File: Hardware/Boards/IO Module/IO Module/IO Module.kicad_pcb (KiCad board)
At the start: 8 copper layers, 50 x 50 mm, 301 parts, among them J1 USB_C_Receptacle, J2 LSHM-130-XX.X-XXX-DV-A-S-K-XX, J3 LSHM-130-XX.X-XXX-DV-A-S-K-XX, J4 HDMI_A, J5 Cam FPC, Q1 IRLML6244, Q2 IRLML6244, SW1 RST, U1 TPS25730D, U10 74LVC1G97, U11 93LCxxBxxOT, U12 74AVC2T245GU, U13 FT600Q, U14 W25Q16JVUXIQ TR, U15 RP2040, U16 TPS74801AWDRC, U17 TUSB542, U18 TUSB8041, U19 TPS74801AWDRC, U2 INA700AYWFR, U20 SN75DP159RGZ, U21 TXB0108DQSR, U22 TXB0101DCK, U23 SN65DPHY440SS, U3 TPSM33625RDNR, U4 TPD2EUSB30A, U5 TPD4EUSB30, U6 TPSM33625RDNR, U7 TPD4EUSB30, U8 74AVC4T774BQX, U9 FT2232HQ, Y1 12Mhz, Y2 30Mhz, Y3 12Mhz, Y4 24Mhz

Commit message: PCB Layout Started
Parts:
- added R103: 1.6K, Resistor_SMD:R_0402_1005Metric, F.Cu at (36.5, 160.0)
- J1: footprint Connector_USB:USB_C_Receptacle_Amphenol_12401548E4-2A -> Connector_USB:USB_C_Receptacle_Amphenol_12401610E4-2A
- J2, J3: moved to B.Cu
- moved U17 130.3 mm to (152.0, 105.0), turned to 90 degrees
- moved U18 125.8 mm to (163.4, 106.4)
- moved J3 123.1 mm to (173.0, 96.0), turned to 90 degrees
- moved J1 119.8 mm to (152.0, 116.0)
- moved U7 109.2 mm to (154.7, 108.2), turned to -90 degrees
- moved U4 108.9 mm to (152.0, 108.3), turned to 180 degrees
- moved U5 106.8 mm to (149.3, 108.3), turned to -90 degrees
- moved U1 97.4 mm to (141.6, 113.1)
- moved J2 84.2 mm to (131.0, 96.0), turned to -90 degrees
- moved TP4 74.9 mm to (174.8, 118.8)
- moved U23 71.3 mm to (163.6, 81.4), turned to 90 degrees
- moved J5 69.7 mm to (162.0, 74.7), turned to 180 degrees
- moved J4 68.4 mm to (142.0, 77.7), turned to 90 degrees
- moved U20 67.2 mm to (140.1, 88.6), turned to 90 degrees
- moved TP2 64.9 mm to (174.8, 73.2)
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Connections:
- U13 pad 21: (no net) -> Net-(U13-RREF)

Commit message: Updated SCH with notes & annotations
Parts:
- removed Q2: IRLML6244, Package_TO_SOT_SMD:SOT-23
- removed U17: TUSB542, IO_Module:TUSB542
- added C149: 100nF, Capacitor_SMD:C_0402_1005Metric, F.Cu at (193.3, 121.5)
- added C150: 100nF, Capacitor_SMD:C_0402_1005Metric, F.Cu at (193.3, 123.5)
- added C151: 100nF, Capacitor_SMD:C_0402_1005Metric, F.Cu at (193.3, 125.4)
- added C152: 100nF, Capacitor_SMD:C_0402_1005Metric, F.Cu at (193.3, 127.4)
- added R104: 1K, Resistor_SMD:R_0402_1005Metric, F.Cu at (184.6, 121.5)
- added R105: 1K, Resistor_SMD:R_0402_1005Metric, F.Cu at (184.6, 123.5)
- added R106: 1K, Resistor_SMD:R_0402_1005Metric, F.Cu at (184.6, 125.5)
- added R107: 1K, Resistor_SMD:R_0402_1005Metric, F.Cu at (184.6, 127.5)
- added R108: 1K, Resistor_SMD:R_0402_1005Metric, F.Cu at (184.6, 129.5)
- added R109: 1K, Resistor_SMD:R_0402_1005Metric, F.Cu at (187.5, 121.5)
- added R110: 1K, Resistor_SMD:R_0402_1005Metric, F.Cu at (187.5, 123.5)
- added R111: 1K, Resistor_SMD:R_0402_1005Metric, F.Cu at (187.5, 125.5)
- added R112: 1K, Resistor_SMD:R_0402_1005Metric, F.Cu at (187.5, 127.5)
- added R113: 1K, Resistor_SMD:R_0402_1005Metric, F.Cu at (187.5, 129.5)
- added R114: 1K, Resistor_SMD:R_0402_1005Metric, F.Cu at (190.4, 121.5)
- added R115: 1K, Resistor_SMD:R_0402_1005Metric, F.Cu at (190.4, 123.5)
- added R116: 1K, Resistor_SMD:R_0402_1005Metric, F.Cu at (190.4, 125.5)
- added R117: 1K, Resistor_SMD:R_0402_1005Metric, F.Cu at (190.4, 127.5)
- added U24: TUSB1142, IO_Module:WQFN_142RNQT_TEX, F.Cu at (155.7, 103.6)
- C101, C102, C103, C105, C106, C107, C108, C94: value 100nF -> 220nF
- C109: value 1uF -> 10uF; footprint Capacitor_SMD:C_0402_1005Metric -> Capacitor_SMD:C_0603_1608Metric
- J1: footprint Connector_USB:USB_C_Receptacle_Amphenol_12401610E4-2A -> IO_Module:GCT_USB4056-03-A_REVA2
- R64, R65, R66, R69: value 10K -> 1K
- moved U3 151.8 mm to (184.2, 115.6)
- moved U6 151.8 mm to (190.1, 115.6)
- moved U10 134.5 mm to (195.8, 101.0), turned to 90 degrees
- moved C108 131.6 mm to (164.1, 108.1), turned to 90 degrees
- moved C102 130.9 mm to (160.3, 108.0), turned to 90 degrees
- moved C107 130.8 mm to (163.4, 108.1), turned to 90 degrees
- moved C105 130.7 mm to (159.7, 108.0), turned to 90 degrees
- moved U12 129.5 mm to (190.4, 95.0), turned to 180 degrees
- moved U2 128.1 mm to (170.7, 110.5), turned to 180 degrees
- moved U8 126.7 mm to (196.7, 105.2), turned to -90 degrees
- moved C106 123.3 mm to (151.8, 107.8), turned to -90 degrees
- moved C94 123.1 mm to (149.7, 107.8), turned to -90 degrees
- moved C103 121.9 mm to (151.2, 107.8), turned to -90 degrees
- moved C101 120.8 mm to (150.3, 107.8), turned to -90 degrees
- moved Y2 120.4 mm to (142.0, 116.5), turned to 90 degrees
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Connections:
- C109 pad 1: +1V8 -> +3V3
- J2 pad 34: /Top/B2B/FIFO_BE0 -> GND
- J2 pad 36: /Top/B2B/FIFO_BE1 -> GND
- J3 pad 01: /Top/B2B/FIFO_CLK -> /Top/B2B/FIFO_BE0
- J3 pad 03: /Top/B2B/FIFO_D0 -> /Top/B2B/FIFO_BE1
- J3 pad 05: /Top/B2B/FIFO_D1 -> /Top/B2B/FIFO_CLK
- J3 pad 07: /Top/B2B/FIFO_D2 -> /Top/B2B/FIFO_D0
- J3 pad 09: /Top/B2B/FIFO_D3 -> /Top/B2B/FIFO_D1
- J3 pad 11: /Top/B2B/FIFO_D4 -> /Top/B2B/FIFO_D2
- J3 pad 13: /Top/B2B/FIFO_D5 -> /Top/B2B/FIFO_D3
- J3 pad 15: /Top/B2B/FIFO_D6 -> /Top/B2B/FIFO_D4
- J3 pad 17: /Top/B2B/FIFO_D7 -> /Top/B2B/FIFO_D5
- J3 pad 19: GND -> /Top/B2B/FIFO_D6
- J3 pad 21: /Top/B2B/MBUS_D0 -> /Top/B2B/FIFO_D7
- J3 pad 23: /Top/B2B/MBUS_D1 -> GND
- J3 pad 25: /Top/B2B/MBUS_D2 -> /Top/B2B/MBUS_D0
- J3 pad 27: /Top/B2B/MBUS_D3 -> /Top/B2B/MBUS_D1
- J3 pad 29: /Top/B2B/MBUS_D4 -> /Top/B2B/MBUS_D2
- J3 pad 31: /Top/B2B/MBUS_D5 -> /Top/B2B/MBUS_D3
- J3 pad 33: /Top/B2B/MBUS_D6 -> /Top/B2B/MBUS_D4
- J3 pad 35: /Top/B2B/MBUS_D7 -> /Top/B2B/MBUS_D5
- J3 pad 37: GND -> /Top/B2B/MBUS_D6
- J3 pad 39: /Top/B2B/MIPI_D0_P -> /Top/B2B/MBUS_D7
- J3 pad 41: /Top/B2B/MIPI_D0_N -> GND
- J3 pad 43: GND -> /Top/B2B/MIPI_D0_P
- J3 pad 45: /Top/B2B/MIPI_D1_P -> /Top/B2B/MIPI_D0_N
- J3 pad 47: /Top/B2B/MIPI_D1_N -> GND
- J3 pad 49: GND -> /Top/B2B/MIPI_D1_P
- J3 pad 51: /Top/B2B/MIPI_CLK_P -> /Top/B2B/MIPI_D1_N
- J3 pad 53: /Top/B2B/MIPI_CLK_N -> GND
- J3 pad 55: GND -> /Top/B2B/MIPI_CLK_P
- J3 pad 57: GND -> /Top/B2B/MIPI_CLK_N
- J4 pad 1: /Top/HDMI/HDMI_C_D2_P -> /Top/HDMI/HDMI_CON_D2_P
- J4 pad 10: /Top/HDMI/HDMI_C_CLK_P -> /Top/HDMI/HDMI_CON_CLK_P
- J4 pad 12: /Top/HDMI/HDMI_C_CLK_N -> /Top/HDMI/HDMI_CON_CLK_N
- J4 pad 3: /Top/HDMI/HDMI_C_D2_N -> /Top/HDMI/HDMI_CON_D2_N
- J4 pad 4: /Top/HDMI/HDMI_C_D1_P -> /Top/HDMI/HDMI_CON_D1_P
- J4 pad 6: /Top/HDMI/HDMI_C_D1_N -> /Top/HDMI/HDMI_CON_D1_N
- J4 pad 7: /Top/HDMI/HDMI_C_D0_P -> /Top/HDMI/HDMI_CON_D0_P
- J4 pad 9: /Top/HDMI/HDMI_C_D0_N -> /Top/HDMI/HDMI_CON_D0_N
- R64 pad 1: Net-(U17-CFG_B2) -> GND
- R64 pad 2: +1V8 -> /Top/USB Hub/USSEQ1
- R65 pad 1: Net-(Q2-D) -> /Top/USB Hub/USSEQ1
- R65 pad 2: +1V8 -> +3V3
- R66 pad 1: GND -> /Top/USB Hub/USSEQ0
- R66 pad 2: Net-(U17-CFG_B2) -> +3V3
- R69 pad 2: /Top/MCU/USBPD_PLG_FLIP -> /Top/USB Hub/USSEQ0
- U20 pad 25: /Top/HDMI/HDMI_C_CLK_N -> /Top/HDMI/HDMI_CON_CLK_N
- U20 pad 26: /Top/HDMI/HDMI_C_CLK_P -> /Top/HDMI/HDMI_CON_CLK_P
- U20 pad 28: /Top/HDMI/HDMI_C_D0_N -> /Top/HDMI/HDMI_CON_D0_N
- U20 pad 29: /Top/HDMI/HDMI_C_D0_P -> /Top/HDMI/HDMI_CON_D0_P
- U20 pad 31: /Top/HDMI/HDMI_C_D1_N -> /Top/HDMI/HDMI_CON_D1_N
- U20 pad 32: /Top/HDMI/HDMI_C_D1_P -> /Top/HDMI/HDMI_CON_D1_P
- U20 pad 34: /Top/HDMI/HDMI_C_D2_N -> /Top/HDMI/HDMI_CON_D2_N
- U20 pad 35: /Top/HDMI/HDMI_C_D2_P -> /Top/HDMI/HDMI_CON_D2_P
- U5 pad 1: /Top/Power/USB3_RX1_P -> /Top/Power/USB3_TX1_N
- U5 pad 10: /Top/Power/USB3_RX1_P -> /Top/Power/USB3_TX1_N
- U5 pad 2: /Top/Power/USB3_RX1_N -> /Top/Power/USB3_TX1_P
- U5 pad 4: /Top/Power/USB3_TX1_P -> /Top/Power/USB3_RX1_N
- U5 pad 5: /Top/Power/USB3_TX1_N -> /Top/Power/USB3_RX1_P
- U5 pad 6: /Top/Power/USB3_TX1_N -> /Top/Power/USB3_RX1_P
- U5 pad 7: /Top/Power/USB3_TX1_P -> /Top/Power/USB3_RX1_N
- U5 pad 9: /Top/Power/USB3_RX1_N -> /Top/Power/USB3_TX1_P
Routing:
- net GND: track 0.00 -> 0.39 mm, vias 0 -> 1
- added copper zone on In1.Cu, net (none)
- added copper zone on In3.Cu, net (none)
- added copper zone on In4.Cu, net (none)
- added copper zone on In6.Cu, net (none)

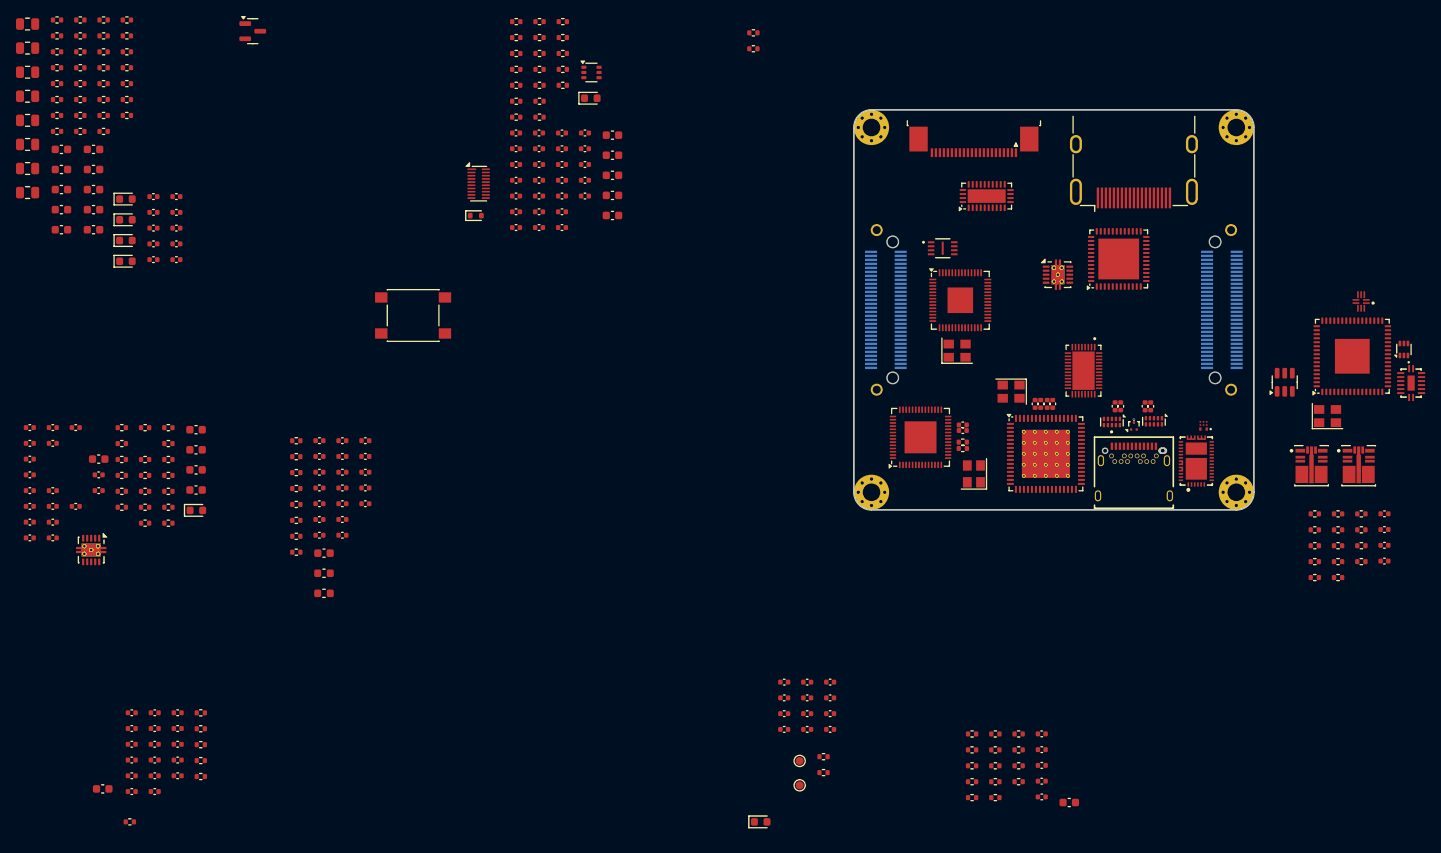
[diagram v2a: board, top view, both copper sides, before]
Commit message: Updated PCB routing for IO Module
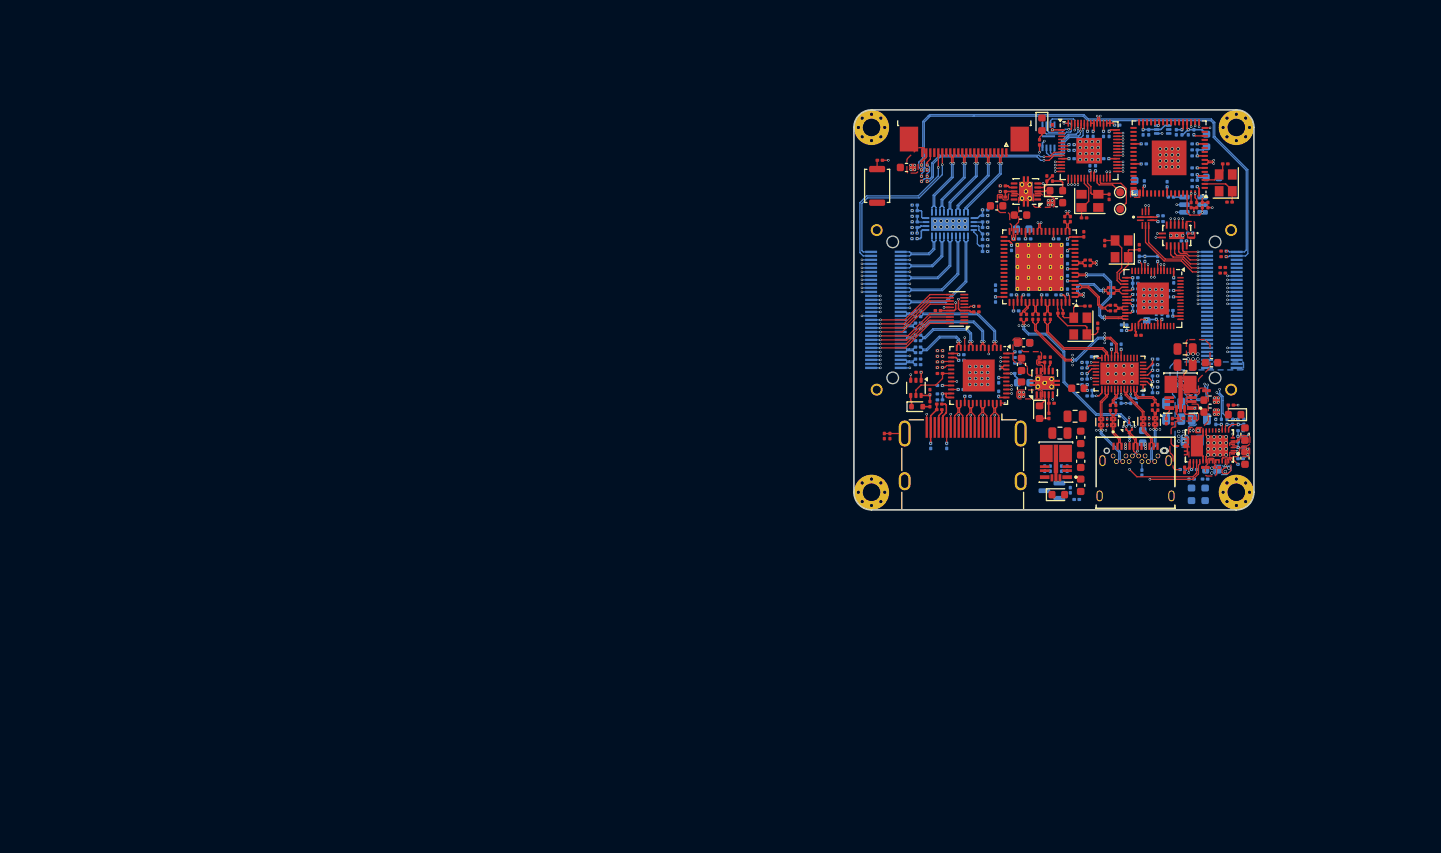
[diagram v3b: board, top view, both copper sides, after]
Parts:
- C1, C118, C12, C124, C42, C49, C5, C6, C7, C8, C84, D1, D4, FB1, FB2, Q1, U10, U11, U14, U2, U23: moved to B.Cu
- C10, C104, C11, C113, C119, C120, C121, C122, C123, C125, C126, C127, C128, C132, C133, C134, C135, C136, C137, C138, C139, C140, C143, C144, C145, C146, C147, C149, C150, C151, C152, C24, C28, C29, C30, C31, C32, C33, C34, C35, C36, C37, C38, C39, C40, C41, C43, C44, C47, C48, C50, C51, C52, C53, C54, C55, C56, C57, C58, C59, C60, C61, C62, C63, C67, C69, C70, C71, C72, C75, C76, C85, C86, C87, C88, C89, C9, C90, C91, C92, C96, C97, C98, C99: footprint Capacitor_SMD:C_0402_1005Metric -> Capacitor_SMD:C_0201_0603Metric; moved to B.Cu
- C100, C101, C102, C103, C105, C106, C107, C108, C110, C111, C112, C117, C129, C130, C131, C141, C142, C17, C2, C21, C3, C4, C45, C46, C64, C65, C66, C74, C77, C78, C79, C83, C93, C94, C95: footprint Capacitor_SMD:C_0402_1005Metric -> Capacitor_SMD:C_0201_0603Metric
- C68, C73: value 100nF -> 1uF; footprint Capacitor_SMD:C_0402_1005Metric -> Capacitor_SMD:C_0201_0603Metric; moved to B.Cu
- R1, R100, R101, R102, R2, R24, R25, R26, R27, R38, R39, R40, R41, R47, R48, R49, R50, R51, R52, R53, R55, R57, R58, R59, R61, R62, R63, R67, R68, R70, R71, R72, R73, R74, R76, R79, R80, R83, R84, R85, R86, R88, R99: footprint Resistor_SMD:R_0402_1005Metric -> Resistor_SMD:R_0201_0603Metric
- R10, R103, R104, R105, R106, R107, R108, R109, R11, R110, R111, R112, R113, R114, R115, R116, R117, R12, R13, R14, R15, R16, R17, R18, R19, R20, R21, R22, R23, R28, R29, R3, R30, R31, R32, R33, R34, R35, R36, R37, R4, R42, R43, R44, R45, R46, R5, R54, R56, R6, R60, R64, R65, R66, R69, R7, R75, R77, R78, R8, R81, R82, R87, R89, R9, R90, R91, R92, R93, R94, R95, R96, R97, R98: footprint Resistor_SMD:R_0402_1005Metric -> Resistor_SMD:R_0201_0603Metric; moved to B.Cu
- SW1: footprint Button_Switch_SMD:SW_SPST_PTS645 -> Button_Switch_SMD:SW_Push_SPST_NO_Alps_SKRK
- moved R11 154.6 mm to (175.3, 113.2)
- moved R12 154.1 mm to (175.3, 113.9), turned to 180 degrees
- moved C6 153.6 mm to (170.2, 109.7)
- moved R10 153.5 mm to (175.3, 114.6)
- moved R13 153.0 mm to (175.3, 112.5), turned to 180 degrees
- moved R14 152.2 mm to (175.3, 111.8)
- moved C8 151.8 mm to (169.3, 112.3)
- moved C13 151.7 mm to (175.9, 114.5), turned to -90 degrees
- moved C5 151.5 mm to (167.0, 109.7), turned to 180 degrees
- moved R9 151.2 mm to (173.6, 110.0), turned to 90 degrees
- moved R19 151.1 mm to (175.7, 110.0), turned to -90 degrees
- moved R8 151.0 mm to (172.9, 110.0), turned to 90 degrees
- moved R15 150.8 mm to (175.0, 110.0), turned to 90 degrees
- moved C14 150.6 mm to (175.9, 111.5), turned to 90 degrees
- moved R22 150.5 mm to (175.3, 115.3), turned to 180 degrees
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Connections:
- net /Top/USB Hub/SPL_S0 renamed /Top/USB Hub/SLP_S0
- net Net-(U15-GPIO25) renamed /Top/MCU/MCU_HB_LED
- net Net-(U18-GRSTz) renamed /Top/USB Hub/USB_HUB_RST
- net Net-(U18-USB_R1) renamed /Top/USB Hub/USB_HUB_REF
- net Net-(U24-MODE) renamed /Top/USB Hub/UMUX_MODE
- net Net-(U24-VIO_SEL) renamed /Top/USB Hub/UMUX_VIO
- C50 pad 1: /Top/USB-FIFO/FT600_VCORE -> /Top/MCU/VMCU_1V1
- C67 pad 1: /Top/MCU/MCU_1V1 -> /Top/USB-JTAG/FT2232_VCORE
- C68 pad 1: /Top/MCU/MCU_1V1 -> /Top/MCU/VMCU_1V1
- C69 pad 1: /Top/MCU/MCU_1V1 -> /Top/MCU/VMCU_1V1
- J1 pad B10: /Top/Power/USB3_RX1_N -> /Top/Power/USB3_RX1_P
- J1 pad B11: /Top/Power/USB3_RX1_P -> /Top/Power/USB3_RX1_N
- J2 pad 01: /Top/PP_VUSB -> /Top/B2B/JTAG_TMS
- J2 pad 02: /Top/PP_VUSB -> /Top/B2B/FPGA_I2C_SCL
- J2 pad 03: /Top/PP_VUSB -> /Top/B2B/JTAG_TCK
- J2 pad 04: /Top/PP_VUSB -> /Top/B2B/FPGA_I2C_SDA
- J2 pad 05: GND -> /Top/B2B/JTAG_TDO
- J2 pad 07: GND -> /Top/B2B/JTAG_TDI
- J2 pad 08: GND -> /Top/B2B/USB_SYSMON_D_P
- J2 pad 09: /Top/B2B/JTAG_TMS -> /Top/B2B/UART_RX
- J2 pad 10: /Top/B2B/USB_SYSMON_D_P -> /Top/B2B/USB_SYSMON_D_N
- J2 pad 11: /Top/B2B/JTAG_TCK -> /Top/B2B/UART_TX
- J2 pad 12: /Top/B2B/USB_SYSMON_D_N -> GND
- J2 pad 13: /Top/B2B/JTAG_TDO -> /Top/B2B/MBUS_D0
- J2 pad 14: GND -> /Top/B2B/MBUS_D8
- J2 pad 15: /Top/B2B/JTAG_TDI -> /Top/B2B/MBUS_D1
- J2 pad 16: GND -> /Top/B2B/MBUS_D9
- J2 pad 17: /Top/B2B/UART_RX -> /Top/B2B/MBUS_D2
- J2 pad 18: GND -> /Top/B2B/MBUS_D10
- J2 pad 19: /Top/B2B/UART_TX -> /Top/B2B/MBUS_D3
- J2 pad 20: /Top/B2B/FT600_RST -> /Top/B2B/MBUS_D11
- J2 pad 21: GND -> /Top/B2B/MBUS_D4
- J2 pad 22: /Top/B2B/FT600_WAKEUP -> /Top/B2B/MBUS_D12
- J2 pad 23: /Top/B2B/HDMI_D2_N -> /Top/B2B/MBUS_D5
- J2 pad 24: /Top/B2B/FT600_OE -> /Top/B2B/MBUS_D13
- J2 pad 25: /Top/B2B/HDMI_D2_P -> /Top/B2B/MBUS_D6
- J2 pad 26: /Top/B2B/FT600_RD -> /Top/B2B/MBUS_D14
- J2 pad 27: GND -> /Top/B2B/MBUS_D7
- J2 pad 28: /Top/B2B/FT600_WR -> /Top/B2B/MBUS_D15
- J2 pad 29: /Top/B2B/HDMI_D1_N -> GND
- J2 pad 30: /Top/B2B/FT600_TXE -> GND
- J2 pad 31: /Top/B2B/HDMI_D1_P -> /Top/B2B/FIFO_BE0
- J2 pad 32: /Top/B2B/FT600_RXE -> /Top/B2B/FIFO_D15
- J2 pad 33: GND -> /Top/B2B/FIFO_BE1
- J2 pad 34: GND -> /Top/B2B/FIFO_D14
- J2 pad 35: /Top/B2B/HDMI_D0_N -> /Top/B2B/FIFO_CLK
- J2 pad 36: GND -> /Top/B2B/FIFO_D13
- J2 pad 37: /Top/B2B/HDMI_D0_P -> /Top/B2B/FIFO_D7
- J2 pad 38: GND -> /Top/B2B/FIFO_D12
- J2 pad 39: GND -> /Top/B2B/FIFO_D6
- J2 pad 40: /Top/B2B/HDMI_SWAP -> /Top/B2B/FIFO_D11
- J2 pad 41: /Top/B2B/HDMI_CLK_N -> /Top/B2B/FIFO_D5
- J2 pad 42: /Top/B2B/HDMI_I2C_EN -> /Top/B2B/FIFO_D10
- J2 pad 43: /Top/B2B/HDMI_CLK_P -> /Top/B2B/FIFO_D4
- J2 pad 44: /Top/B2B/HDMI_PRE_SEL -> /Top/B2B/FIFO_D9
- J2 pad 45: GND -> /Top/B2B/FIFO_D3
- J2 pad 46: /Top/B2B/HDMI_EQ_SEL -> /Top/B2B/FIFO_D8
- J2 pad 47: /Top/B2B/HDMI_AUX_N -> /Top/B2B/FIFO_D2
- J2 pad 48: /Top/B2B/HDMI_SEL -> GND
- J2 pad 49: /Top/B2B/HDMI_AUX_P -> /Top/B2B/FIFO_D1
- J2 pad 50: /Top/B2B/HDMI_TX_TERM_CTL -> /Top/B2B/FT600_RD
- J2 pad 51: GND -> /Top/B2B/FIFO_D0
- J2 pad 52: /Top/B2B/HDMI_CEC_EN -> /Top/B2B/FT600_WR
- J2 pad 53: /Top/B2B/FPGA_I2C_SCL -> GND
- J2 pad 54: /Top/B2B/HDMI_SLEW_CTL -> GND
- J2 pad 55: /Top/B2B/FPGA_I2C_SDA -> GND
- J2 pad 56: /Top/B2B/HDMI_OE -> GND
- J2 pad 57: /Top/B2B/HDMI_SCL_SRC -> /Top/PP_VUSB
- J2 pad 58: /Top/B2B/HDMI_HPD_SRC -> /Top/PP_VUSB
- J2 pad 59: /Top/B2B/HDMI_SDA_SRC -> /Top/PP_VUSB
- J2 pad 60: /Top/B2B/HDMI_CEC -> /Top/PP_VUSB
- J3 pad 01: /Top/B2B/FIFO_BE0 -> GND
- J3 pad 02: /Top/B2B/FIFO_D8 -> /Top/B2B/HDMI_SDA_SRC
- J3 pad 03: /Top/B2B/FIFO_BE1 -> /Top/B2B/HDMI_AUX_N
- J3 pad 04: /Top/B2B/FIFO_D9 -> /Top/B2B/HDMI_SCL_SRC
- J3 pad 05: /Top/B2B/FIFO_CLK -> /Top/B2B/HDMI_AUX_P
- J3 pad 06: /Top/B2B/FIFO_D10 -> /Top/B2B/HDMI_OE
- J3 pad 07: /Top/B2B/FIFO_D0 -> GND
- J3 pad 08: /Top/B2B/FIFO_D11 -> /Top/B2B/HDMI_HPD_SRC
- J3 pad 09: /Top/B2B/FIFO_D1 -> /Top/B2B/HDMI_CLK_N
- J3 pad 10: /Top/B2B/FIFO_D12 -> /Top/B2B/HDMI_CEC
- J3 pad 11: /Top/B2B/FIFO_D2 -> /Top/B2B/HDMI_CLK_P
- J3 pad 12: /Top/B2B/FIFO_D13 -> /Top/B2B/HDMI_SWAP
- J3 pad 13: /Top/B2B/FIFO_D3 -> GND
- J3 pad 14: /Top/B2B/FIFO_D14 -> /Top/B2B/HDMI_I2C_EN
- J3 pad 15: /Top/B2B/FIFO_D4 -> /Top/B2B/HDMI_D0_N
- J3 pad 16: /Top/B2B/FIFO_D15 -> /Top/B2B/HDMI_PRE_SEL
- J3 pad 17: /Top/B2B/FIFO_D5 -> /Top/B2B/HDMI_D0_P
- J3 pad 18: GND -> /Top/B2B/HDMI_EQ_SEL
- J3 pad 19: /Top/B2B/FIFO_D6 -> GND
- J3 pad 20: /Top/B2B/MBUS_D8 -> /Top/B2B/HDMI_SEL
- J3 pad 21: /Top/B2B/FIFO_D7 -> /Top/B2B/HDMI_D1_N
- J3 pad 22: /Top/B2B/MBUS_D9 -> /Top/B2B/HDMI_TX_TERM_CTL
- J3 pad 23: GND -> /Top/B2B/HDMI_D1_P
- J3 pad 24: /Top/B2B/MBUS_D10 -> /Top/B2B/HDMI_CEC_EN
- J3 pad 25: /Top/B2B/MBUS_D0 -> GND
- J3 pad 26: /Top/B2B/MBUS_D11 -> /Top/B2B/HDMI_SLEW_CTL
- J3 pad 27: /Top/B2B/MBUS_D1 -> /Top/B2B/HDMI_D2_N
- J3 pad 28: /Top/B2B/MBUS_D12 -> GND
- J3 pad 29: /Top/B2B/MBUS_D2 -> /Top/B2B/HDMI_D2_P
- J3 pad 30: /Top/B2B/MBUS_D13 -> /Top/B2B/FT600_RXE
- J3 pad 31: /Top/B2B/MBUS_D3 -> GND
- J3 pad 32: /Top/B2B/MBUS_D14 -> /Top/B2B/FT600_TXE
- J3 pad 33: /Top/B2B/MBUS_D4 -> /Top/B2B/MIPI_D0_P
- J3 pad 34: /Top/B2B/MBUS_D15 -> /Top/B2B/FT600_OE
- J3 pad 35: /Top/B2B/MBUS_D5 -> /Top/B2B/MIPI_D0_N
- J3 pad 36: GND -> /Top/B2B/FT600_WAKEUP
- J3 pad 37: /Top/B2B/MBUS_D6 -> GND
- J3 pad 38: /Top/B2B/MIPI_D2_P -> /Top/B2B/FT600_RST
- J3 pad 39: /Top/B2B/MBUS_D7 -> /Top/B2B/MIPI_D1_P
- J3 pad 40: /Top/B2B/MIPI_D2_N -> GND
- J3 pad 41: GND -> /Top/B2B/MIPI_D1_N
- J3 pad 43: /Top/B2B/MIPI_D0_P -> GND
- J3 pad 44: /Top/B2B/MIPI_D3_P -> GND
- J3 pad 45: /Top/B2B/MIPI_D0_N -> /Top/B2B/MIPI_CLK_P
- J3 pad 46: /Top/B2B/MIPI_D3_N -> GND
- J3 pad 47: GND -> /Top/B2B/MIPI_CLK_N
- J3 pad 49: /Top/B2B/MIPI_D1_P -> GND
- J3 pad 50: /Top/B2B/CAM_PWR_EN -> GND
- J3 pad 51: /Top/B2B/MIPI_D1_N -> /Top/B2B/MIPI_D2_P
- J3 pad 52: /Top/B2B/CAM_LED_EN -> GND
- J3 pad 53: GND -> /Top/B2B/MIPI_D2_N
- J3 pad 55: /Top/B2B/MIPI_CLK_P -> GND
- J3 pad 57: /Top/B2B/MIPI_CLK_N -> /Top/B2B/MIPI_D3_P
- J3 pad 58: GND -> /Top/B2B/CAM_LED_EN
- J3 pad 59: GND -> /Top/B2B/MIPI_D3_N
- J3 pad 60: GND -> /Top/B2B/CAM_PWR_EN
- R41 pad 1: /Top/USB-JTAG/FT2232_EPROM_DO -> /Top/USB-JTAG/FT2232_EPROM_DI
- U15 pad 23: /Top/MCU/MCU_1V1 -> /Top/MCU/VMCU_1V1
- U15 pad 45: /Top/MCU/MCU_1V1 -> /Top/MCU/VMCU_1V1
- U15 pad 50: /Top/MCU/MCU_1V1 -> /Top/MCU/VMCU_1V1
- U5 pad 4: /Top/Power/USB3_RX1_N -> /Top/Power/USB3_RX1_P
- U5 pad 5: /Top/Power/USB3_RX1_P -> /Top/Power/USB3_RX1_N
- U5 pad 6: /Top/Power/USB3_RX1_P -> /Top/Power/USB3_RX1_N
- U5 pad 7: /Top/Power/USB3_RX1_N -> /Top/Power/USB3_RX1_P
- U7 pad 1: /Top/Power/USB3_RX2_P -> /Top/Power/USB3_TX2_P
- U7 pad 10: /Top/Power/USB3_RX2_P -> /Top/Power/USB3_TX2_P
- U7 pad 2: /Top/Power/USB3_RX2_N -> /Top/Power/USB3_TX2_N
- U7 pad 4: /Top/Power/USB3_TX2_P -> /Top/Power/USB3_RX2_P
- U7 pad 5: /Top/Power/USB3_TX2_N -> /Top/Power/USB3_RX2_N
- U7 pad 6: /Top/Power/USB3_TX2_N -> /Top/Power/USB3_RX2_N
- U7 pad 7: /Top/Power/USB3_TX2_P -> /Top/Power/USB3_RX2_P
- U7 pad 9: /Top/Power/USB3_RX2_N -> /Top/Power/USB3_TX2_N
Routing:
- net /Top/B2B/FPGA_I2C_SDA: track 0.00 -> 64.7 mm, vias 0 -> 3
- net +3V3: track 0.00 -> 64.2 mm, vias 0 -> 58
- net /Top/B2B/FPGA_I2C_SCL: track 0.00 -> 63.4 mm, vias 0 -> 3
- net GND: track 0.39 -> 28.9 mm, vias 1 -> 171
- net /Top/Power/USB2_D_N: track 0.00 -> 26.7 mm, vias 0 -> 3
- net /Top/Power/USB2_D_P: track 0.00 -> 26.6 mm, vias 0 -> 2
- net /Top/B2B/CAM_LED_EN: track 0.00 -> 21.9 mm, vias 0 -> 1
- net /Top/B2B/CAM_PWR_EN: track 0.00 -> 21.4 mm, vias 0 -> 1
- net /Top/Camera FPC/I2C1_SDA: track 0.00 -> 20.2 mm, vias 0 -> 3
- net /Top/Camera FPC/I2C1_SCL: track 0.00 -> 19.5 mm, vias 0 -> 3
- net /Top/USB Hub/TXA_P: track 0.00 -> 16.5 mm, vias 0 -> 2
- net /Top/USB Hub/TXA_N: track 0.00 -> 16.5 mm, vias 0 -> 2
- net /Top/B2B/MIPI_D0_P: track 0.00 -> 15.2 mm
- net /Top/B2B/MIPI_D0_N: track 0.00 -> 14.9 mm
- net /Top/USB Hub/USB_FIFO_RX_P: track 0.00 -> 13.3 mm, vias 0 -> 2
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- added copper zone on F.Cu, net +1V1
- added copper zone on F.Cu, net +1V8
- added copper zone on F.Cu, net +3V3
- added copper zone on F.Cu, net /Top/HDMI/PP_1V1_HDMI
- added copper zone on B.Cu, net /Top/PP_VUSB
- added copper zone on F.Cu, net /Top/Power/LDO_1V5
- added copper zone on F.Cu, net /Top/Power/LDO_3V3
- added copper zone on B.Cu, net /Top/Power/PP_VUSB_R
- added copper zone on F.Cu, net /Top/Power/PP_VUSB_R
- added copper zone on F.Cu, net /Top/Power/VBUS_IN
- added copper zone on B.Cu, net /Top/Power/VIN_3V3
- added copper zone on F.Cu, net /Top/Power/VIN_3V3
- added copper zone on F.Cu, net /Top/USB-JTAG/FT2232_VCORE
- added copper zone on F.Cu, net GND
